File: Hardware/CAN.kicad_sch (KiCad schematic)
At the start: 12 parts, among them J3 Conn_01x02_Pin, J4 PeripheralCAN, J5 PeripheralCAN, U4 TCAN337, U5 CDSOT23-T24CAN

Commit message: something changed idk what though
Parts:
- renumbered C21 to C28, C22 to C29, D8 to D10, J3 to J4, J4 to J5, J5 to J6, R12 to R17, R13 to R18, R14 to R19, U4 to U5, U5 to U6
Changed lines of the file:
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@@
 		(on_board yes)
 		(dnp no)
-		(property "Reference" "#PWR057"
+		(property "Reference" "#PWR074"
 			(at 50.8 88.9 0)
 			(effects
@@
 			(project "BPS-AmperesPCB"
 				(path "/a452d214-ea00-440d-a445-5d6103fda43a/2dff07b6-7dab-4ebe-8bad-c03f5c351937"
-					(reference "#PWR057")
+					(reference "#PWR074")
 					(unit 1)
 				)
@@
 		(on_board yes)
 		(dnp no)
-		(property "Reference" "C21"
+		(property "Reference" "C28"
 			(at 101.6 38.735 0)
 			(effects
@@
 			(project "BPS-AmperesPCB"
 				(path "/a452d214-ea00-440d-a445-5d6103fda43a/2dff07b6-7dab-4ebe-8bad-c03f5c351937"
-					(reference "C21")
+					(reference "C28")
 					(unit 1)
 				)
@@
 		(on_board yes)
 		(dnp no)
-		(property "Reference" "R13"
+		(property "Reference" "R18"
 			(at 22.352 37.9984 0)
 			(effects
@@
 			(project "BPS-AmperesPCB"
 				(path "/a452d214-ea00-440d-a445-5d6103fda43a/2dff07b6-7dab-4ebe-8bad-c03f5c351937"
-					(reference "R13")
+					(reference "R18")
 					(unit 1)
 				)
@@
 		(on_board yes)
 		(dnp no)
-		(property "Reference" "R14"
+		(property "Reference" "R19"
 			(at 75.438 76.2 90)
 			(effects
@@
 			(project "BPS-AmperesPCB"
 				(path "/a452d214-ea00-440d-a445-5d6103fda43a/2dff07b6-7dab-4ebe-8bad-c03f5c351937"
-					(reference "R14")
+					(reference "R19")
 					(unit 1)
 				)
@@
 		(on_board yes)
 		(dnp no)
-		(property "Reference" "#PWR053"
+		(property "Reference" "#PWR070"
 			(at 127 55.88 0)
 			(effects
@@
 			(project "BPS-AmperesPCB"
 				(path "/a452d214-ea00-440d-a445-5d6103fda43a/2dff07b6-7dab-4ebe-8bad-c03f5c351937"
-					(reference "#PWR053")
+					(reference "#PWR070")
 					(unit 1)
 				)
@@
 		(on_board yes)
 		(dnp no)
-		(property "Reference" "J3"
+		(property "Reference" "J4"
 			(at 107.95 69.85 0)
 			(effects
@@
 			(project "BPS-AmperesPCB"
 				(path "/a452d214-ea00-440d-a445-5d6103fda43a/2dff07b6-7dab-4ebe-8bad-c03f5c351937"
-					(reference "J3")
+					(reference "J4")
 					(unit 1)
 				)
@@
 		(on_board yes)
 		(dnp no)
-		(property "Reference" "U5"
+		(property "Reference" "U6"
 			(at 39.37 72.39 0)
 			(effects
@@
 			(project "BPS-AmperesPCB"
 				(path "/a452d214-ea00-440d-a445-5d6103fda43a/2dff07b6-7dab-4ebe-8bad-c03f5c351937"
-					(reference "U5")
+					(reference "U6")
 					(unit 1)
 				)
@@
 		(dnp no)
 		(fields_autoplaced yes)
-		(property "Reference" "D8"
+		(property "Reference" "D10"
 			(at 130.81 44.7674 90)
 			(effects
@@
 			(project ""
 				(path "/a452d214-ea00-440d-a445-5d6103fda43a/2dff07b6-7dab-4ebe-8bad-c03f5c351937"
-					(reference "D8")
+					(reference "D10")
 					(unit 1)
 				)
@@
 		(on_board yes)
 		(dnp no)
-		(property "Reference" "#PWR050"
+		(property "Reference" "#PWR067"
 			(at 24.13 36.83 0)
 			(effects
@@
 			(project "BPS-AmperesPCB"
 				(path "/a452d214-ea00-440d-a445-5d6103fda43a/2dff07b6-7dab-4ebe-8bad-c03f5c351937"
-					(reference "#PWR050")
+					(reference "#PWR067")
 					(unit 1)
 				)
@@
 		(dnp no)
 		(fields_autoplaced yes)
-		(property "Reference" "C22"
+		(property "Reference" "C29"
 			(at 114.3 38.735 0)
 			(effects
@@
 			(project "BPS-AmperesPCB"
 				(path "/a452d214-ea00-440d-a445-5d6103fda43a/2dff07b6-7dab-4ebe-8bad-c03f5c351937"
-					(reference "C22")
+					(reference "C29")
 					(unit 1)
 				)
@@
 		(dnp no)
 		(fields_autoplaced yes)
-		(property "Reference" "U4"
+		(property "Reference" "U5"
 			(at 68.1833 27.94 0)
 			(effects
@@
 			(project "BPS-AmperesPCB"
 				(path "/a452d214-ea00-440d-a445-5d6103fda43a/2dff07b6-7dab-4ebe-8bad-c03f5c351937"
-					(reference "U4")
+					(reference "U5")
 					(unit 1)
 				)
@@
 		(dnp no)
 		(fields_autoplaced yes)
-		(property "Reference" "#PWR055"
+		(property "Reference" "#PWR072"
 			(at 147.32 80.01 0)
 			(effects
@@
 			(project "BPS-AmperesPCB"
 				(path "/a452d214-ea00-440d-a445-5d6103fda43a/2dff07b6-7dab-4ebe-8bad-c03f5c351937"
-					(reference "#PWR055")
+					(reference "#PWR072")
 					(unit 1)
 				)
@@
 		(on_board yes)
 		(dnp no)
-		(property "Reference" "#PWR049"
+		(property "Reference" "#PWR066"
 			(at 66.04 31.75 0)
 			(effects
@@
 			(project "BPS-AmperesPCB"
 				(path "/a452d214-ea00-440d-a445-5d6103fda43a/2dff07b6-7dab-4ebe-8bad-c03f5c351937"
-					(reference "#PWR049")
+					(reference "#PWR066")
 					(unit 1)
 				)
@@
 		(on_board yes)
 		(dnp no)
-		(property "Reference" "#PWR052"
+		(property "Reference" "#PWR069"
 			(at 104.14 50.8 0)
 			(effects
@@
 			(project "BPS-AmperesPCB"
 				(path "/a452d214-ea00-440d-a445-5d6103fda43a/2dff07b6-7dab-4ebe-8bad-c03f5c351937"
-					(reference "#PWR052")
+					(reference "#PWR069")
 					(unit 1)
 				)
@@
 		(dnp no)
 		(fields_autoplaced yes)
-		(property "Reference" "J5"
+		(property "Reference" "J6"
 			(at 160.655 72.39 0)
 			(effects
@@
 			(project "BPS-AmperesPCB"
 				(path "/a452d214-ea00-440d-a445-5d6103fda43a/2dff07b6-7dab-4ebe-8bad-c03f5c351937"
-					(reference "J5")
+					(reference "J6")
 					(unit 1)
 				)
@@
 		(on_board yes)
 		(dnp no)
-		(property "Reference" "#PWR054"
+		(property "Reference" "#PWR071"
 			(at 66.04 58.42 0)
 			(effects
@@
 			(project "BPS-AmperesPCB"
 				(path "/a452d214-ea00-440d-a445-5d6103fda43a/2dff07b6-7dab-4ebe-8bad-c03f5c351937"
-					(reference "#PWR054")
+					(reference "#PWR071")
 					(unit 1)
 				)
@@
 		(dnp no)
 		(fields_autoplaced yes)
-		(property "Reference" "J4"
+		(property "Reference" "J5"
 			(at 127.635 72.39 0)
 			(effects
@@
 			(project "BPS-AmperesPCB"
 				(path "/a452d214-ea00-440d-a445-5d6103fda43a/2dff07b6-7dab-4ebe-8bad-c03f5c351937"
-					(reference "J4")
+					(reference "J5")
 					(unit 1)
 				)
@@
 		(dnp no)
 		(fields_autoplaced yes)
-		(property "Reference" "#PWR056"
+		(property "Reference" "#PWR073"
 			(at 180.34 80.01 0)
 			(effects
@@
 			(project "BPS-AmperesPCB"
 				(path "/a452d214-ea00-440d-a445-5d6103fda43a/2dff07b6-7dab-4ebe-8bad-c03f5c351937"
-					(reference "#PWR056")
+					(reference "#PWR073")
 					(unit 1)
 				)
@@
 		(on_board yes)
 		(dnp no)
-		(property "Reference" "#PWR051"
+		(property "Reference" "#PWR068"
 			(at 104.14 38.1 0)
 			(effects
@@
 			(project "BPS-AmperesPCB"
 				(path "/a452d214-ea00-440d-a445-5d6103fda43a/2dff07b6-7dab-4ebe-8bad-c03f5c351937"
-					(reference "#PWR051")
+					(reference "#PWR068")
 					(unit 1)
 				)
@@
 		(dnp no)
 		(fields_autoplaced yes)
-		(property "Reference" "#PWR059"
+		(property "Reference" "#PWR076"
 			(at 180.34 92.71 0)
 			(effects
@@
 			(project "BPS-AmperesPCB"
 				(path "/a452d214-ea00-440d-a445-5d6103fda43a/2dff07b6-7dab-4ebe-8bad-c03f5c351937"
-					(reference "#PWR059")
+					(reference "#PWR076")
 					(unit 1)
 				)
@@
 		(dnp no)
 		(fields_autoplaced yes)
-		(property "Reference" "#PWR058"
+		(property "Reference" "#PWR075"
 			(at 147.32 92.71 0)
 			(effects
@@
 			(project "BPS-AmperesPCB"
 				(path "/a452d214-ea00-440d-a445-5d6103fda43a/2dff07b6-7dab-4ebe-8bad-c03f5c351937"
-					(reference "#PWR058")
+					(reference "#PWR075")
 					(unit 1)
 				)
@@
 		(on_board yes)
 		(dnp no)
-		(property "Reference" "R12"
+		(property "Reference" "R17"
 			(at 128.778 34.3916 0)
 			(effects
@@
 			(project "BPS-AmperesPCB"
 				(path "/a452d214-ea00-440d-a445-5d6103fda43a/2dff07b6-7dab-4ebe-8bad-c03f5c351937"
-					(reference "R12")
-					(unit 1)
-				)
+					(reference "R17")
+					(unit 1)
+				)

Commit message: 0603 footprints
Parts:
- C28, C29: footprint Capacitor_SMD:C_0805_2012Metric -> Capacitor_SMD:C_0603_1608Metric_Pad1.08x0.95mm_HandSolder
- D10: footprint (none) -> LED_SMD:LED_0603_1608Metric_Pad1.05x0.95mm_HandSolder
- R17, R18, R19: footprint Resistor_SMD:R_0805_2012Metric -> Resistor_SMD:R_0603_1608Metric_Pad0.98x0.95mm_HandSolder
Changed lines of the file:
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@@
+	)
+	(symbol
+		(lib_id "utsvt-connectors:PeripheralCANConnector")
+		(at 127 82.55 0)
+		(unit 1)
+		(exclude_from_sim no)
+		(in_bom yes)
+		(on_board yes)
+		(dnp no)
+		(fields_autoplaced yes)
+		(property "Reference" "J5"
+			(at 127.635 72.39 0)
+			(effects
+				(font
+					(size 1.524 1.524)
+				)
+			)
+		)
+		(property "Value" "PeripheralCAN"
+			(at 127.635 74.93 0)
+			(effects
+				(font
+					(size 1.524 1.524)
+				)
+			)
+		)
+		(property "Footprint" "UTSVT_Connectors:Molex_Nano-Fit_105309-xx04_1x04_P2.50mm_Vertical"
+			(at 127 91.44 0)
+			(effects
+				(font
+					(size 1.524 1.524)
+				)
+				(hide yes)
+			)
+		)
+		(property "Datasheet" "https://www.mouser.com/ProductDetail/Molex/105309-1204?qs=PqFvFmEiOr6mDAWV2BJKbg%3D%3D&srsltid=AfmBOopk7YsqdMLo2_DAHKaHKt3Hg126ooPXYWv5Q2Pfx6rW7DaYZCT2"
+			(at 132.08 74.93 0)
+			(effects
+				(font
+					(size 1.524 1.524)
+				)
+				(hide yes)
+			)
+		)
+		(property "Description" "Connection to the car's Peripheral CAN bus."
+			(at 127 82.55 0)
+			(effects
+				(font
+					(size 1.27 1.27)
+				)
+				(hide yes)
+			)
+		)
+		(property "P/N" "105309-1204 "
+			(at 127 82.55 0)
+			(effects
+				(font
+					(size 1.27 1.27)
+				)
+				(hide yes)
+			)
+		)
+		(pin "4"
+		)
+		(pin "1"
+		)
+		(pin "3"
+		)
+		(pin "2"
+		)
+		(instances
+			(project ""
+				(path "/a452d214-ea00-440d-a445-5d6103fda43a/2dff07b6-7dab-4ebe-8bad-c03f5c351937"
+					(reference "J5")
+					(unit 1)
+				)
+			)
+		)
 	)
 	(symbol
@@
 			)
 		)
-		(property "Footprint" "Capacitor_SMD:C_0805_2012Metric"
+		(property "Footprint" "Capacitor_SMD:C_0603_1608Metric_Pad1.08x0.95mm_HandSolder"
 			(at 98.7552 43.18 0)
 			(effects
@@
 			)
 		)
-		(property "Footprint" "Resistor_SMD:R_0805_2012Metric"
+		(property "Footprint" "Resistor_SMD:R_0603_1608Metric_Pad0.98x0.95mm_HandSolder"
 			(at 25.908 36.83 90)
 			(effects
@@
 			)
 		)
-		(property "Footprint" "Resistor_SMD:R_0805_2012Metric"
+		(property "Footprint" "Resistor_SMD:R_0603_1608Metric_Pad0.98x0.95mm_HandSolder"
 			(at 79.248 76.2 90)
 			(effects
@@
 	)
 	(symbol
+		(lib_id "utsvt-connectors:PeripheralCANConnector")
+		(at 160.02 82.55 0)
+		(unit 1)
+		(exclude_from_sim no)
+		(in_bom yes)
+		(on_board yes)
+		(dnp no)
+		(fields_autoplaced yes)
+		(property "Reference" "J6"
+			(at 160.655 72.39 0)
+			(effects
+				(font
+					(size 1.524 1.524)
+				)
+			)
+		)
+		(property "Value" "PeripheralCAN"
+			(at 160.655 74.93 0)
+			(effects
+				(font
+					(size 1.524 1.524)
+				)
+			)
+		)
+		(property "Footprint" "UTSVT_Connectors:Molex_Nano-Fit_105309-xx04_1x04_P2.50mm_Vertical"
+			(at 160.02 91.44 0)
+			(effects
+				(font
+					(size 1.524 1.524)
+				)
+				(hide yes)
+			)
+		)
+		(property "Datasheet" "https://www.mouser.com/ProductDetail/Molex/105309-1204?qs=PqFvFmEiOr6mDAWV2BJKbg%3D%3D&srsltid=AfmBOopk7YsqdMLo2_DAHKaHKt3Hg126ooPXYWv5Q2Pfx6rW7DaYZCT2"
+			(at 165.1 74.93 0)
+			(effects
+				(font
+					(size 1.524 1.524)
+				)
+				(hide yes)
+			)
+		)
+		(property "Description" "Connection to the car's Peripheral CAN bus."
+			(at 160.02 82.55 0)
+			(effects
+				(font
+					(size 1.27 1.27)
+				)
+				(hide yes)
+			)
+		)
+		(property "P/N" "105309-1204 "
+			(at 160.02 82.55 0)
+			(effects
+				(font
+					(size 1.27 1.27)
+				)
+				(hide yes)
+			)
+		)
+		(pin "4"
+		)
+		(pin "1"
+		)
+		(pin "3"
+		)
+		(pin "2"
+		)
+		(instances
+			(project "BPS-AmperesPCB"
+				(path "/a452d214-ea00-440d-a445-5d6103fda43a/2dff07b6-7dab-4ebe-8bad-c03f5c351937"
+					(reference "J6")
+					(unit 1)
+				)
+			)
+		)
+	)
+	(symbol
 		(lib_id "Connector:Conn_01x02_Pin")
 		(at 107.95 77.47 180)
@@
 			)
 		)
-		(property "Footprint" ""
+		(property "Footprint" "LED_SMD:LED_0603_1608Metric_Pad1.05x0.95mm_HandSolder"
 			(at 127 44.45 0)
 			(effects
@@
 			)
 		)
-		(property "Footprint" "Capacitor_SMD:C_0805_2012Metric"
+		(property "Footprint" "Capacitor_SMD:C_0603_1608Metric_Pad1.08x0.95mm_HandSolder"
 			(at 111.4552 43.18 0)
 			(effects
@@
 	)
 	(symbol
-		(lib_id "utsvt-connectors:PeripheralCANConnector")
-		(at 160.02 82.55 0)
-		(unit 1)
-		(exclude_from_sim no)
-		(in_bom yes)
-		(on_board yes)
-		(dnp no)
-		(fields_autoplaced yes)
-		(property "Reference" "J6"
-			(at 160.655 72.39 0)
-			(effects
-				(font
-					(size 1.524 1.524)
-				)
-			)
-		)
-		(property "Value" "PeripheralCAN"
-			(at 160.655 74.93 0)
-			(effects
-				(font
-					(size 1.524 1.524)
-				)
-			)
-		)
-		(property "Footprint" "UTSVT_Connectors:Molex_Nano-Fit_105309-xx04_1x04_P2.50mm_Vertical"
-			(at 160.02 91.44 0)
-			(effects
-				(font
-					(size 1.524 1.524)
-				)
-				(hide yes)
-			)
-		)
-		(property "Datasheet" "https://www.mouser.com/ProductDetail/Molex/105309-1204?qs=PqFvFmEiOr6mDAWV2BJKbg%3D%3D&srsltid=AfmBOopk7YsqdMLo2_DAHKaHKt3Hg126ooPXYWv5Q2Pfx6rW7DaYZCT2"
-			(at 165.1 74.93 0)
-			(effects
-				(font
-					(size 1.524 1.524)
-				)
-				(hide yes)
-			)
-		)
-		(property "Description" "Connection to the car's Peripheral CAN bus."
-			(at 160.02 82.55 0)
-			(effects
-				(font
-					(size 1.27 1.27)
-				)
-				(hide yes)
-			)
-		)
-		(property "P/N" "105309-1204 "
-			(at 160.02 82.55 0)
-			(effects
-				(font
-					(size 1.27 1.27)
-				)
-				(hide yes)
-			)
-		)
-		(pin "3"
-		)
-		(pin "4"
-		)
-		(pin "1"
-		)
-		(pin "2"
-		)
-		(instances
-			(project "BPS-AmperesPCB"
-				(path "/a452d214-ea00-440d-a445-5d6103fda43a/2dff07b6-7dab-4ebe-8bad-c03f5c351937"
-					(reference "J6")
-					(unit 1)
-				)
-			)
-		)
-	)
-	(symbol
 		(lib_id "power:GND")
 		(at 66.04 52.07 0)
@@
 				(path "/a452d214-ea00-440d-a445-5d6103fda43a/2dff07b6-7dab-4ebe-8bad-c03f5c351937"
 					(reference "#PWR071")
-					(unit 1)
-				)
-			)
-		)
-	)
-	(symbol
-		(lib_id "utsvt-connectors:PeripheralCANConnector")
-		(at 127 82.55 0)
-		(unit 1)
-		(exclude_from_sim no)
-		(in_bom yes)
-		(on_board yes)
-		(dnp no)
-		(fields_autoplaced yes)
-		(property "Reference" "J5"
-			(at 127.635 72.39 0)
-			(effects
-				(font
-					(size 1.524 1.524)
-				)
-			)
-		)
-		(property "Value" "PeripheralCAN"
-			(at 127.635 74.93 0)
-			(effects
-				(font
-					(size 1.524 1.524)
-				)
-			)
-		)
-		(property "Footprint" "UTSVT_Connectors:Molex_Nano-Fit_105309-xx04_1x04_P2.50mm_Vertical"
-			(at 127 91.44 0)
-			(effects
-				(font
-					(size 1.524 1.524)
-				)
-				(hide yes)
-			)
-		)
-		(property "Datasheet" "https://www.mouser.com/ProductDetail/Molex/105309-1204?qs=PqFvFmEiOr6mDAWV2BJKbg%3D%3D&srsltid=AfmBOopk7YsqdMLo2_DAHKaHKt3Hg126ooPXYWv5Q2Pfx6rW7DaYZCT2"
-			(at 132.08 74.93 0)
-			(effects
-				(font
-					(size 1.524 1.524)
-				)
-				(hide yes)
-			)
-		)
-		(property "Description" "Connection to the car's Peripheral CAN bus."
-			(at 127 82.55 0)
-			(effects
-				(font
-					(size 1.27 1.27)
-				)
-				(hide yes)
-			)
-		)
-		(property "P/N" "105309-1204 "
-			(at 127 82.55 0)
-			(effects
-				(font
-					(size 1.27 1.27)
-				)
-				(hide yes)
-			)
-		)
-		(pin "3"
-		)
-		(pin "4"
-		)
-		(pin "1"
-		)
-		(pin "2"
-		)
-		(instances
-			(project "BPS-AmperesPCB"
-				(path "/a452d214-ea00-440d-a445-5d6103fda43a/2dff07b6-7dab-4ebe-8bad-c03f5c351937"
-					(reference "J5")
 					(unit 1)
 				)
@@
 			)
 		)
-		(property "Footprint" "Resistor_SMD:R_0805_2012Metric"
+		(property "Footprint" "Resistor_SMD:R_0603_1608Metric_Pad0.98x0.95mm_HandSolder"
 			(at 125.222 35.56 90)
 			(effects

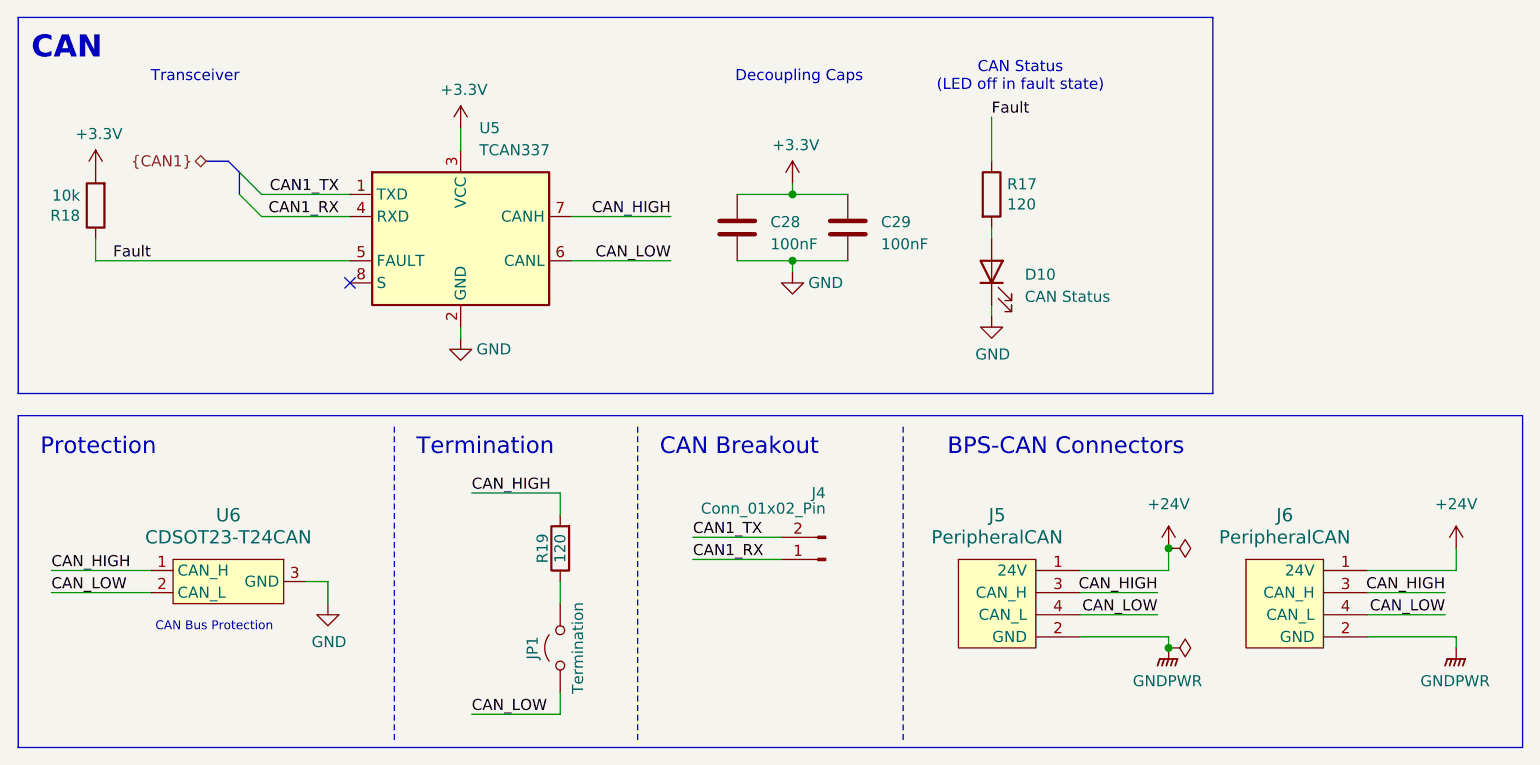
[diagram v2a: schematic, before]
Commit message: 24-5 buck from psom, OR gate for bootload. more sheet organization
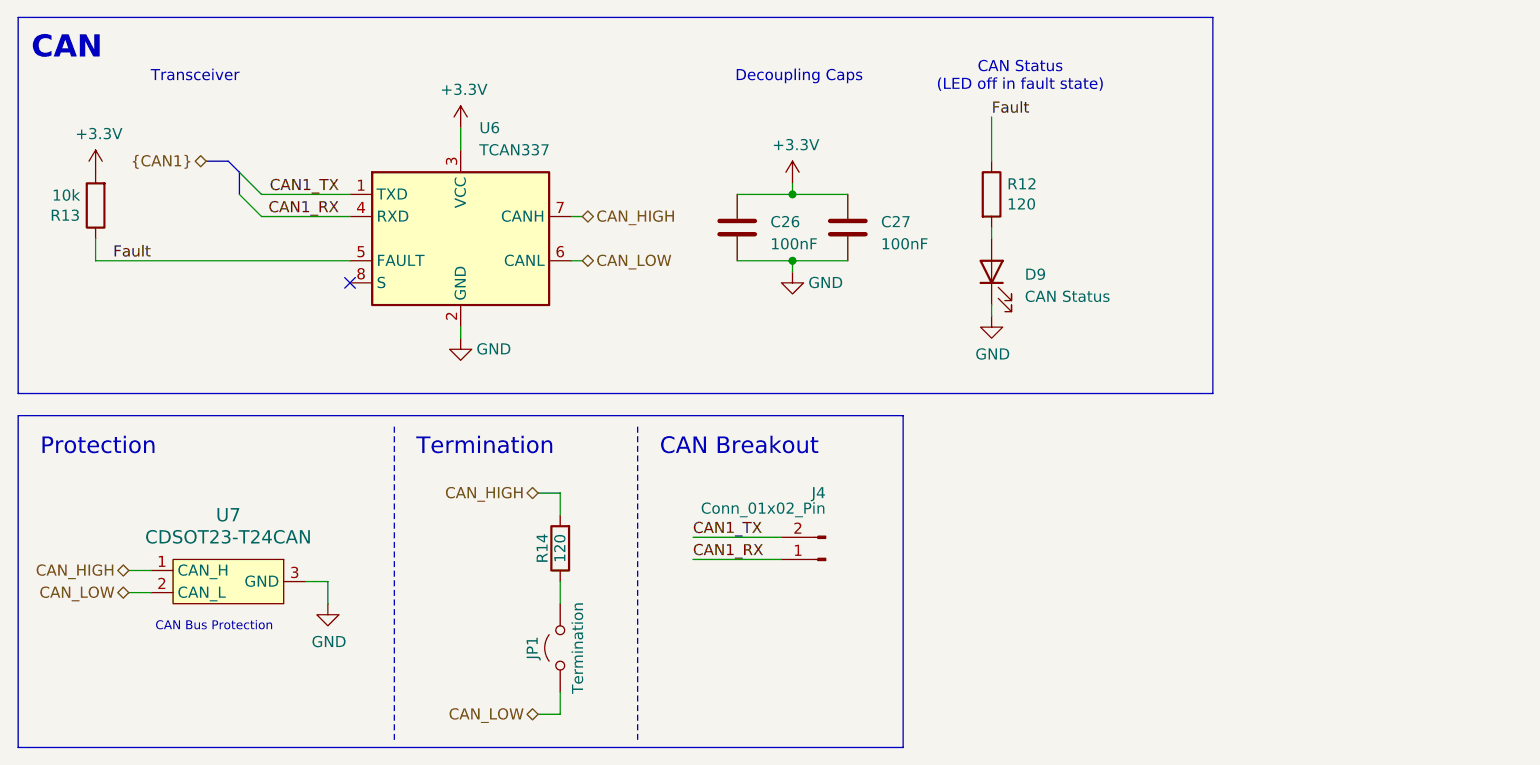
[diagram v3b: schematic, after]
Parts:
- removed J5, J6: PeripheralCAN, UTSVT_Connectors:Molex_Nano-Fit_105309-xx04_1x04_P2.50mm_Vertical, symbol utsvt-connectors:PeripheralCANConnector
- renumbered C28 to C26, C29 to C27, D10 to D9, R17 to R12, R18 to R13, R19 to R14, U5 to U6, U6 to U7
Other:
- note removed: "BPS-CAN Connectors"
